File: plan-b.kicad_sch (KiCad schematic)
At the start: 0 parts

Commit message: Reworking the MCU schematics sheet into QIAA package
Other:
- sheet MCU ports: added 1.8v, 3.3v, VSENSE_ON; removed none
- sheet PSU ports: added 1.8v, VSENSE_ON; removed none
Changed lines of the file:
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@@
+	(wire
+		(pts
+			(xy 143.51 66.04) (xy 151.13 66.04)
+		)
+		(stroke
+			(width 0)
+			(type default)
+		)
+	)
+	(wire
+		(pts
+			(xy 199.39 78.74) (xy 199.39 95.25)
+		)
+		(stroke
+			(width 0)
+			(type default)
+		)
+	)
+	(wire
+		(pts
+			(xy 146.05 91.44) (xy 146.05 95.25)
+		)
+		(stroke
+			(width 0)
+			(type default)
+		)
+	)
+	(wire
+		(pts
+			(xy 217.17 99.06) (xy 220.98 99.06)
+		)
+		(stroke
+			(width 0)
+			(type default)
+		)
+	)
+	(wire
+		(pts
+			(xy 163.83 78.74) (xy 163.83 91.44)
+		)
+		(stroke
+			(width 0)
+			(type default)
+		)
+	)
+	(wire
+		(pts
+			(xy 214.63 78.74) (xy 214.63 101.6)
+		)
+		(stroke
+			(width 0)
+			(type default)
+		)
+	)
+	(wire
+		(pts
+			(xy 212.09 78.74) (xy 212.09 104.14)
+		)
+		(stroke
+			(width 0)
+			(type default)
+		)
+	)
+	(wire
+		(pts
+			(xy 143.51 58.42) (xy 151.13 58.42)
+		)
+		(stroke
+			(width 0)
+			(type default)
+		)
+	)
+	(wire
+		(pts
+			(xy 177.8 78.74) (xy 177.8 95.25)
+		)
+		(stroke
+			(width 0)
+			(type default)
+		)
+	)
+	(wire
+		(pts
+			(xy 212.09 104.14) (xy 220.98 104.14)
+		)
+		(stroke
+			(width 0)
+			(type default)
+		)
+	)
+	(wire
+		(pts
+			(xy 194.31 78.74) (xy 194.31 95.25)
+		)
+		(stroke
+			(width 0)
+			(type default)
+		)
+	)
+	(wire
+		(pts
+			(xy 231.14 86.36) (xy 231.14 63.5)
+		)
+		(stroke
+			(width 0)
+			(type default)
+		)
+	)
+	(wire
+		(pts
+			(xy 227.33 55.88) (xy 234.95 55.88)
+		)
+		(stroke
+			(width 0)
+			(type default)
+		)
+	)
+	(wire
+		(pts
+			(xy 209.55 106.68) (xy 220.98 106.68)
+		)
+		(stroke
+			(width 0)
+			(type default)
+		)
+	)
+	(wire
+		(pts
+			(xy 182.88 78.74) (xy 182.88 95.25)
+		)
+		(stroke
+			(width 0)
+			(type default)
+		)
+	)
 	(wire
 		(pts
@@
 	(wire
 		(pts
-			(xy 199.39 78.74) (xy 199.39 95.25)
-		)
-		(stroke
-			(width 0)
-			(type default)
-		)
-	)
-	(wire
-		(pts
-			(xy 146.05 91.44) (xy 146.05 95.25)
-		)
-		(stroke
-			(width 0)
-			(type default)
-		)
-	)
-	(wire
-		(pts
-			(xy 217.17 99.06) (xy 220.98 99.06)
-		)
-		(stroke
-			(width 0)
-			(type default)
-		)
-	)
-	(wire
-		(pts
-			(xy 163.83 78.74) (xy 163.83 91.44)
-		)
-		(stroke
-			(width 0)
-			(type default)
-		)
-	)
-	(wire
-		(pts
-			(xy 214.63 78.74) (xy 214.63 101.6)
-		)
-		(stroke
-			(width 0)
-			(type default)
-		)
-	)
-	(wire
-		(pts
-			(xy 212.09 78.74) (xy 212.09 104.14)
-		)
-		(stroke
-			(width 0)
-			(type default)
-		)
-	)
-	(wire
-		(pts
-			(xy 143.51 58.42) (xy 151.13 58.42)
-		)
-		(stroke
-			(width 0)
-			(type default)
-		)
-	)
-	(wire
-		(pts
-			(xy 177.8 78.74) (xy 177.8 95.25)
-		)
-		(stroke
-			(width 0)
-			(type default)
-		)
-	)
-	(wire
-		(pts
-			(xy 212.09 104.14) (xy 220.98 104.14)
-		)
-		(stroke
-			(width 0)
-			(type default)
-		)
-	)
-	(wire
-		(pts
-			(xy 194.31 78.74) (xy 194.31 95.25)
-		)
-		(stroke
-			(width 0)
-			(type default)
-		)
-	)
-	(wire
-		(pts
-			(xy 231.14 86.36) (xy 231.14 63.5)
-		)
-		(stroke
-			(width 0)
-			(type default)
-		)
-	)
-	(wire
-		(pts
-			(xy 227.33 55.88) (xy 234.95 55.88)
-		)
-		(stroke
-			(width 0)
-			(type default)
-		)
-	)
-	(wire
-		(pts
-			(xy 209.55 106.68) (xy 220.98 106.68)
-		)
-		(stroke
-			(width 0)
-			(type default)
-		)
-	)
-	(wire
-		(pts
-			(xy 182.88 78.74) (xy 182.88 95.25)
-		)
-		(stroke
-			(width 0)
-			(type default)
-		)
-	)
-	(wire
-		(pts
 			(xy 134.62 78.74) (xy 134.62 95.25)
 		)
@@
 		(pts
 			(xy 180.34 78.74) (xy 180.34 95.25)
+		)
+		(stroke
+			(width 0)
+			(type default)
+		)
+	)
+	(wire
+		(pts
+			(xy 143.51 68.58) (xy 151.13 68.58)
 		)
 		(stroke
@@
 		)
 		(pin "VSYS" input
+			(at 151.13 66.04 180)
+			(effects
+				(font
+					(size 1.27 1.27)
+				)
+				(justify left)
+			)
+		)
+		(pin "1.8v" input
+			(at 151.13 68.58 180)
+			(effects
+				(font
+					(size 1.27 1.27)
+				)
+				(justify left)
+			)
+		)
+		(pin "3.3v" input
+			(at 227.33 66.04 0)
+			(effects
+				(font
+					(size 1.27 1.27)
+				)
+				(justify right)
+			)
+		)
+		(pin "VSENSE_ON" input
 			(at 151.13 63.5 180)
 			(effects
@@
 		)
 		(pin "VSYS" input
-			(at 143.51 63.5 0)
+			(at 143.51 66.04 0)
 			(effects
 				(font
@@
 			)
 		)
+		(pin "1.8v" input
+			(at 143.51 68.58 0)
+			(effects
+				(font
+					(size 1.27 1.27)
+				)
+				(justify right)
+			)
+		)
+		(pin "VSENSE_ON" input
+			(at 143.51 63.5 0)
+			(effects
+				(font
+					(size 1.27 1.27)
+				)
+				(justify right)
+			)
+		)

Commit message: Dumping the reference layouts into the PCB
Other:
- sheet MCU ports: added 1.8v ; removed none
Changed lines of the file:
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@@
 		)
 	)
-	(junction
-		(at 231.14 63.5)
-		(diameter 0)
-		(color 0 0 0 0)
-	)
-	(wire
-		(pts
-			(xy 163.83 91.44) (xy 146.05 91.44)
+	(wire
+		(pts
+			(xy 165.1 91.44) (xy 146.05 91.44)
 		)
 		(stroke
@@
 	(wire
 		(pts
-			(xy 242.57 95.25) (xy 242.57 86.36)
-		)
-		(stroke
-			(width 0)
-			(type default)
-		)
-	)
-	(wire
-		(pts
-			(xy 227.33 63.5) (xy 231.14 63.5)
-		)
-		(stroke
-			(width 0)
-			(type default)
-		)
-	)
-	(wire
-		(pts
-			(xy 143.51 88.9) (xy 161.29 88.9)
+			(xy 143.51 88.9) (xy 162.56 88.9)
 		)
 		(stroke
@@
 	(wire
 		(pts
-			(xy 231.14 63.5) (xy 234.95 63.5)
+			(xy 227.33 60.96) (xy 234.95 60.96)
 		)
 		(stroke
@@
 	(wire
 		(pts
-			(xy 161.29 88.9) (xy 161.29 78.74)
+			(xy 162.56 88.9) (xy 162.56 78.74)
 		)
 		(stroke
@@
 	(wire
 		(pts
+			(xy 143.51 68.58) (xy 151.13 68.58)
+		)
+		(stroke
+			(width 0)
+			(type default)
+		)
+	)
+	(wire
+		(pts
 			(xy 146.05 91.44) (xy 146.05 95.25)
 		)
@@
 	(wire
 		(pts
-			(xy 163.83 78.74) (xy 163.83 91.44)
+			(xy 165.1 78.74) (xy 165.1 91.44)
 		)
 		(stroke
@@
 	(wire
 		(pts
-			(xy 231.14 86.36) (xy 231.14 63.5)
-		)
-		(stroke
-			(width 0)
-			(type default)
-		)
-	)
-	(wire
-		(pts
 			(xy 227.33 55.88) (xy 234.95 55.88)
 		)
@@
 	(wire
 		(pts
-			(xy 242.57 86.36) (xy 231.14 86.36)
-		)
-		(stroke
-			(width 0)
-			(type default)
-		)
-	)
-	(wire
-		(pts
 			(xy 180.34 78.74) (xy 180.34 95.25)
-		)
-		(stroke
-			(width 0)
-			(type default)
-		)
-	)
-	(wire
-		(pts
-			(xy 143.51 68.58) (xy 151.13 68.58)
 		)
 		(stroke
@@
 		)
 		(pin "RGB DATA" input
-			(at 161.29 78.74 270)
+			(at 162.56 78.74 270)
 			(effects
 				(font
@@
 		)
 		(pin "RGB ON" input
-			(at 163.83 78.74 270)
+			(at 165.1 78.74 270)
 			(effects
 				(font
@@
 		)
 		(pin "VDD" input
-			(at 227.33 63.5 0)
+			(at 227.33 60.96 0)
 			(effects
 				(font
@@
 		)
 		(pin "1.8v" input
-			(at 151.13 68.58 180)
+			(at 222.25 78.74 270)
 			(effects
 				(font
@@
 		)
 		(pin "3.3v" input
-			(at 227.33 66.04 0)
-			(effects
-				(font
-					(size 1.27 1.27)
-				)
-				(justify right)
+			(at 219.71 78.74 270)
+			(effects
+				(font
+					(size 1.27 1.27)
+				)
+				(justify left)
 			)
 		)
 		(pin "VSENSE_ON" input
 			(at 151.13 63.5 180)
+			(effects
+				(font
+					(size 1.27 1.27)
+				)
+				(justify left)
+			)
+		)
+		(pin "1.8v " input
+			(at 151.13 68.58 180)
 			(effects
 				(font
@@
 		)
 		(pin "VDD" input
-			(at 234.95 63.5 180)
-			(effects
-				(font
+			(at 234.95 60.96 180)
+			(effects
+				(font

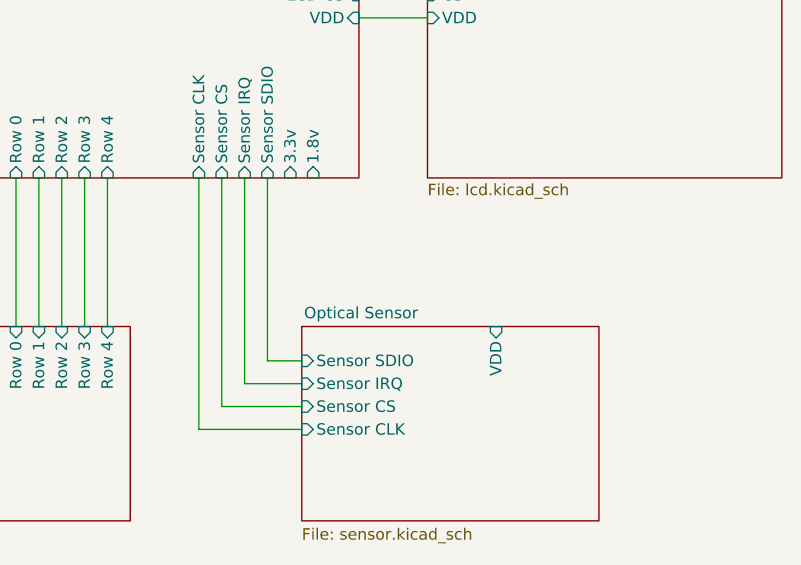
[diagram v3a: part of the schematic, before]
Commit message: Sorting out most of the powerlines
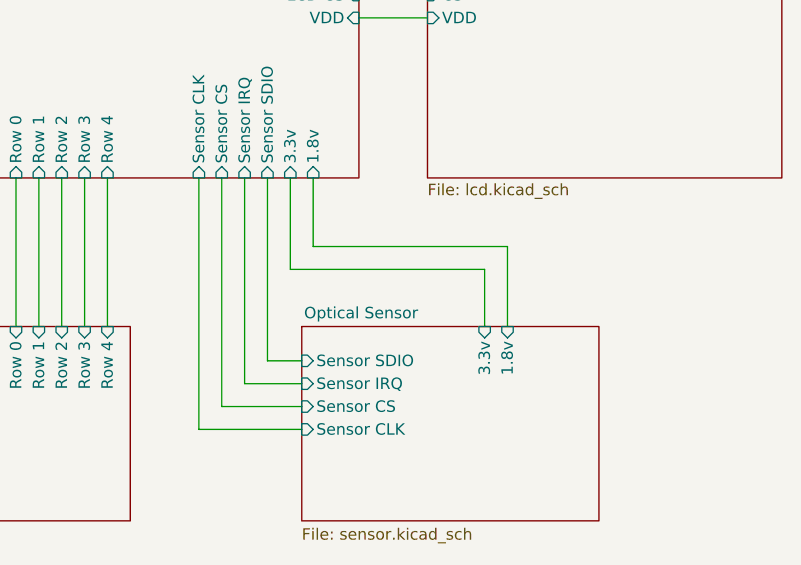
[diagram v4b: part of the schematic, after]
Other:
- sheet Optical Sensor ports: added 1.8v, 3.3v; removed VDD
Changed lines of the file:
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@@
+	(wire
+		(pts
+			(xy 222.25 86.36) (xy 243.84 86.36)
+		)
+		(stroke
+			(width 0)
+			(type default)
+		)
+	)
 	(wire
 		(pts
@@
 	(wire
 		(pts
+			(xy 243.84 86.36) (xy 243.84 95.25)
+		)
+		(stroke
+			(width 0)
+			(type default)
+		)
+	)
+	(wire
+		(pts
+			(xy 219.71 88.9) (xy 241.3 88.9)
+		)
+		(stroke
+			(width 0)
+			(type default)
+		)
+	)
+	(wire
+		(pts
 			(xy 194.31 78.74) (xy 194.31 95.25)
 		)
@@
 	(wire
 		(pts
+			(xy 222.25 78.74) (xy 222.25 86.36)
+		)
+		(stroke
+			(width 0)
+			(type default)
+		)
+	)
+	(wire
+		(pts
+			(xy 219.71 78.74) (xy 219.71 88.9)
+		)
+		(stroke
+			(width 0)
+			(type default)
+		)
+	)
+	(wire
+		(pts
 			(xy 182.88 78.74) (xy 182.88 95.25)
 		)
@@
 		(pts
 			(xy 180.34 78.74) (xy 180.34 95.25)
+		)
+		(stroke
+			(width 0)
+			(type default)
+		)
+	)
+	(wire
+		(pts
+			(xy 241.3 88.9) (xy 241.3 95.25)
 		)
 		(stroke
@@
 			)
 		)
-		(pin "VDD" input
-			(at 242.57 95.25 90)
-			(effects
-				(font
+		(pin "1.8v" input
+			(at 243.84 95.25 90)
+			(effects
+				(font
+					(size 1.27 1.27)
+				)
+				(justify right)
+			)
+		)
+		(pin "3.3v" input
+			(at 241.3 95.25 90)
+			(effects
+				(font

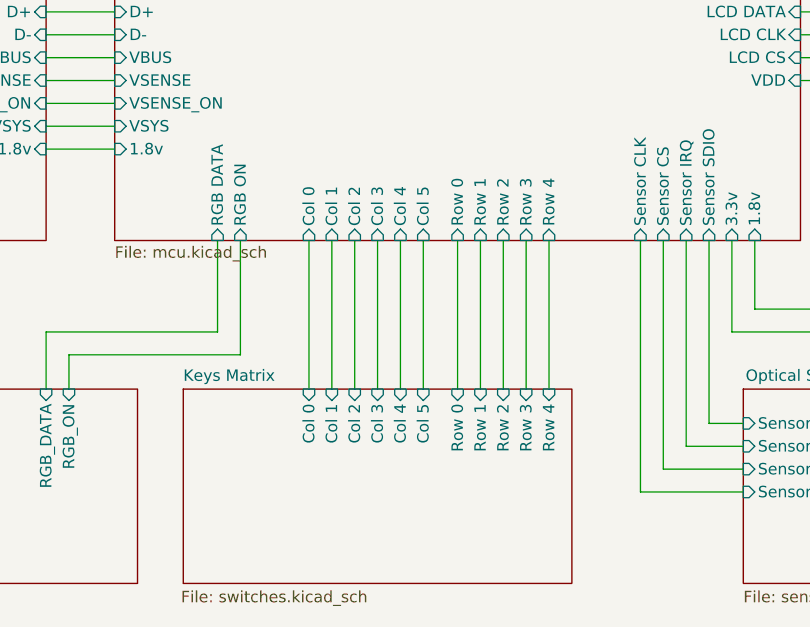
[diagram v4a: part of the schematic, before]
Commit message: Swapping rows connector to the same 6 pins as columns
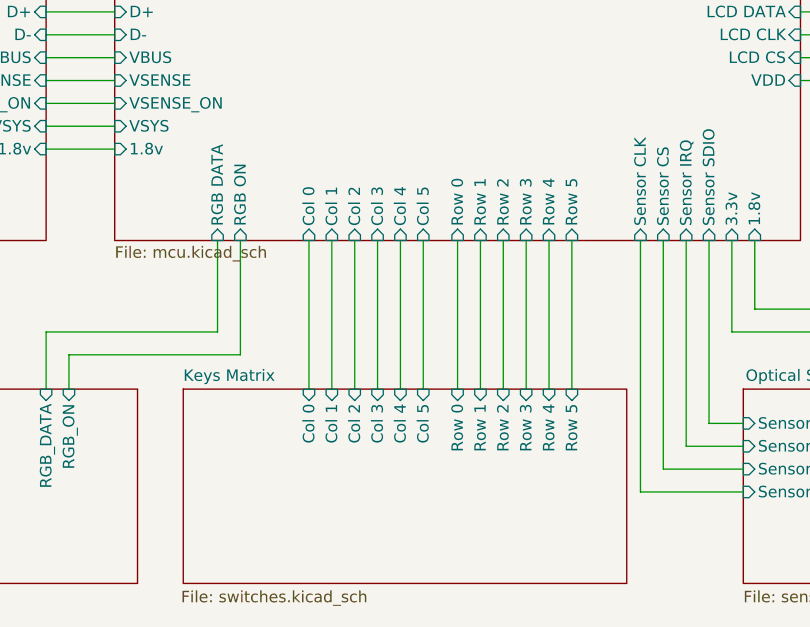
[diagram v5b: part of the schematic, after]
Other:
- sheet Keys Matrix ports: added Row 5; removed none
- sheet MCU ports: added Row 5; removed none
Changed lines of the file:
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@@
+	(wire
+		(pts
+			(xy 201.93 78.74) (xy 201.93 95.25)
+		)
+		(stroke
+			(width 0)
+			(type default)
+		)
+	)
 	(wire
 		(pts
@@
 			)
 		)
+		(pin "Row 5" input
+			(at 201.93 78.74 270)
+			(effects
+				(font
+					(size 1.27 1.27)
+				)
+				(justify left)
+			)
+		)
 		(instances
 			(project "plan-b"
@@
 	(sheet
 		(at 158.75 95.25)
-		(size 43.18 21.59)
+		(size 49.276 21.59)
 		(exclude_from_sim no)
 		(in_bom yes)
@@
 			(effects
 				(font
+					(size 1.27 1.27)
+				)
+				(justify right)
+			)
+		)
+		(pin "Row 5" input
+			(at 201.93 95.25 90)
+			(effects
+				(font

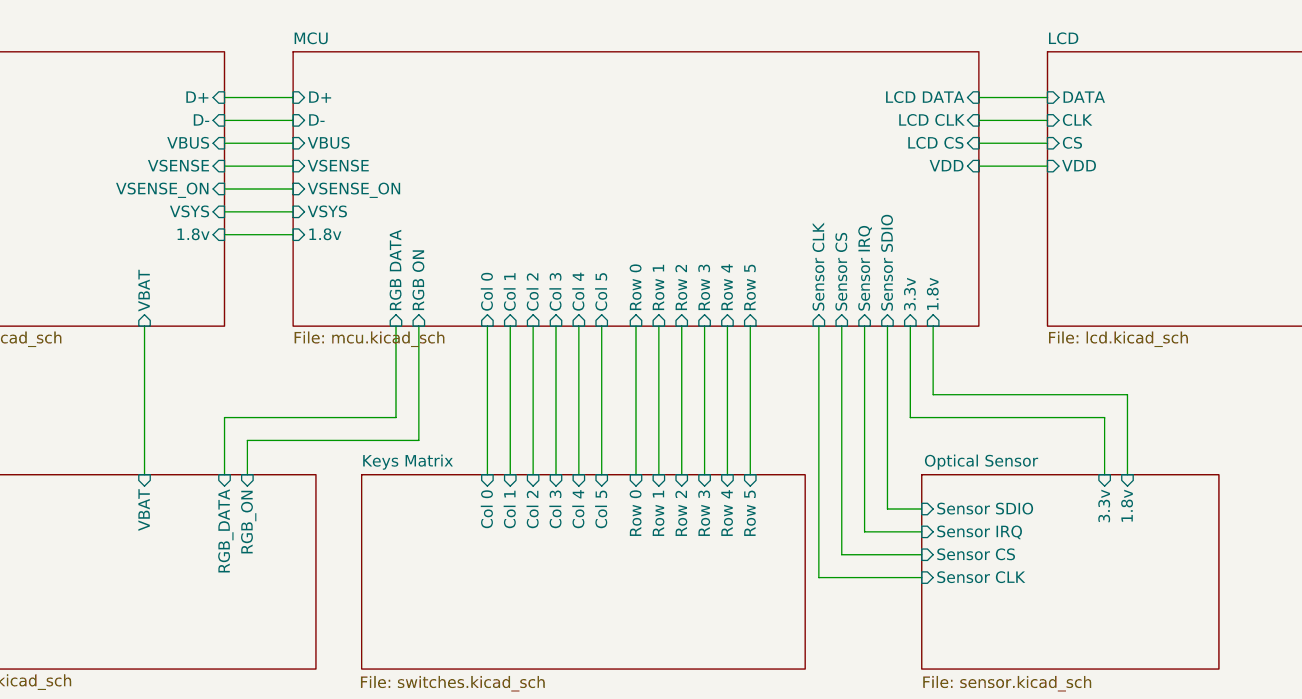
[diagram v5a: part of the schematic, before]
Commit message: Removing the 1.8v power supply option
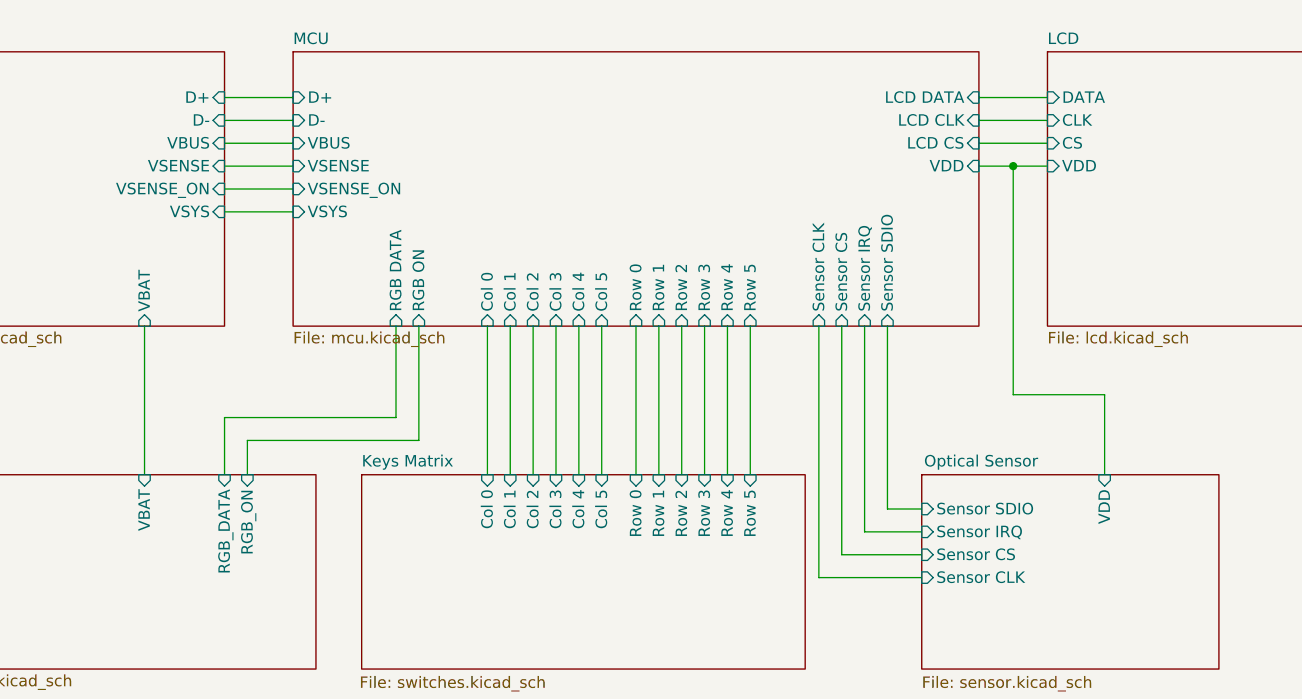
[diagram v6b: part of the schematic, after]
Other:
- sheet MCU ports: added none; removed 1.8v, 1.8v , 3.3v
- sheet Optical Sensor ports: added VDD; removed 1.8v, 3.3v
- sheet PSU ports: added none; removed 1.8v
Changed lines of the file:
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@@
 		)
+	)
+	(junction
+		(at 231.14 60.96)
+		(diameter 0)
+		(color 0 0 0 0)
 	)
 	(wire
@@
 	(wire
 		(pts
-			(xy 227.33 60.96) (xy 234.95 60.96)
+			(xy 227.33 60.96) (xy 231.14 60.96)
 		)
 		(stroke
@@
 	(wire
 		(pts
+			(xy 231.14 86.36) (xy 231.14 60.96)
+		)
+		(stroke
+			(width 0)
+			(type default)
+		)
+	)
+	(wire
+		(pts
 			(xy 143.51 66.04) (xy 151.13 66.04)
 		)
@@
 	(wire
 		(pts
-			(xy 143.51 68.58) (xy 151.13 68.58)
-		)
-		(stroke
-			(width 0)
-			(type default)
-		)
-	)
-	(wire
-		(pts
 			(xy 146.05 91.44) (xy 146.05 95.25)
 		)
@@
 	(wire
 		(pts
-			(xy 222.25 86.36) (xy 243.84 86.36)
+			(xy 241.3 86.36) (xy 231.14 86.36)
 		)
 		(stroke
@@
 	(wire
 		(pts
-			(xy 243.84 86.36) (xy 243.84 95.25)
-		)
-		(stroke
-			(width 0)
-			(type default)
-		)
-	)
-	(wire
-		(pts
-			(xy 219.71 88.9) (xy 241.3 88.9)
+			(xy 231.14 60.96) (xy 234.95 60.96)
 		)
 		(stroke
@@
 	(wire
 		(pts
-			(xy 222.25 78.74) (xy 222.25 86.36)
-		)
-		(stroke
-			(width 0)
-			(type default)
-		)
-	)
-	(wire
-		(pts
-			(xy 219.71 78.74) (xy 219.71 88.9)
-		)
-		(stroke
-			(width 0)
-			(type default)
-		)
-	)
-	(wire
-		(pts
 			(xy 182.88 78.74) (xy 182.88 95.25)
 		)
@@
 	(wire
 		(pts
+			(xy 241.3 95.25) (xy 241.3 86.36)
+		)
+		(stroke
+			(width 0)
+			(type default)
+		)
+	)
+	(wire
+		(pts
 			(xy 172.72 78.74) (xy 172.72 95.25)
 		)
@@
 		(pts
 			(xy 180.34 78.74) (xy 180.34 95.25)
-		)
-		(stroke
-			(width 0)
-			(type default)
-		)
-	)
-	(wire
-		(pts
-			(xy 241.3 88.9) (xy 241.3 95.25)
 		)
 		(stroke
@@
 			)
 		)
-		(pin "1.8v" input
-			(at 222.25 78.74 270)
-			(effects
-				(font
-					(size 1.27 1.27)
-				)
-				(justify left)
-			)
-		)
-		(pin "3.3v" input
-			(at 219.71 78.74 270)
-			(effects
-				(font
-					(size 1.27 1.27)
-				)
-				(justify left)
-			)
-		)
 		(pin "VSENSE_ON" input
 			(at 151.13 63.5 180)
-			(effects
-				(font
-					(size 1.27 1.27)
-				)
-				(justify left)
-			)
-		)
-		(pin "1.8v " input
-			(at 151.13 68.58 180)
 			(effects
 				(font
@@
 			)
 		)
-		(pin "1.8v" input
-			(at 143.51 68.58 0)
-			(effects
-				(font
-					(size 1.27 1.27)
-				)
-				(justify right)
-			)
-		)
 		(pin "VSENSE_ON" input
 			(at 143.51 63.5 0)
@@
 			)
 		)
-		(pin "1.8v" input
-			(at 243.84 95.25 90)
-			(effects
-				(font
-					(size 1.27 1.27)
-				)
-				(justify right)
-			)
-		)
-		(pin "3.3v" input
+		(pin "VDD" input
 			(at 241.3 95.25 90)
 			(effects
